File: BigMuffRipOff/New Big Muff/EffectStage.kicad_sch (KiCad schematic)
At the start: 64 parts, among them Q1 BC549, Q2 BC549, Q3 BC549, Q4 BC549, U1 TPL0501-100DCNR, U2 TPL0501-100DCNR, U3 TPL0501-100DCNR, U4 TL071HIDBVR, U5 TL071HIDBVR, U7 TL071HIDBVR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

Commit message: removed the old diodes from before
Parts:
- removed CR1, CR2: 1N4148W-13-F, 284867-E-footprint:SOD123_DIO, symbol 1N4148:1N4148W-13-F
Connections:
- net at C10.2, C9.1, Q3.1 (C)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: now also C8.1

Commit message: big muff connector fixed i think?
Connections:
- net CS_1 renamed sustain_CS
- net CS_2 renamed tone_CS
- net CS_3 renamed volume_CS_1
- net CS_4 renamed Volume_CS_2
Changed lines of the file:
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@@
 		)
 	)
-	(hierarchical_label "CS_1"
+	(hierarchical_label "sustain_CS"
 		(shape input)
 		(at 134.62 85.09 180)
@@
 		)
 	)
-	(hierarchical_label "CS_2"
+	(hierarchical_label "tone_CS"
 		(shape input)
 		(at 356.87 72.39 180)
@@
 		)
 	)
-	(hierarchical_label "CS_4"
+	(hierarchical_label "Volume_CS_2"
 		(shape input)
 		(at 447.04 143.51 180)
@@
 		)
 	)
-	(hierarchical_label "CS_3"
+	(hierarchical_label "volume_CS_1"
 		(shape input)
 		(at 445.77 90.17 180)

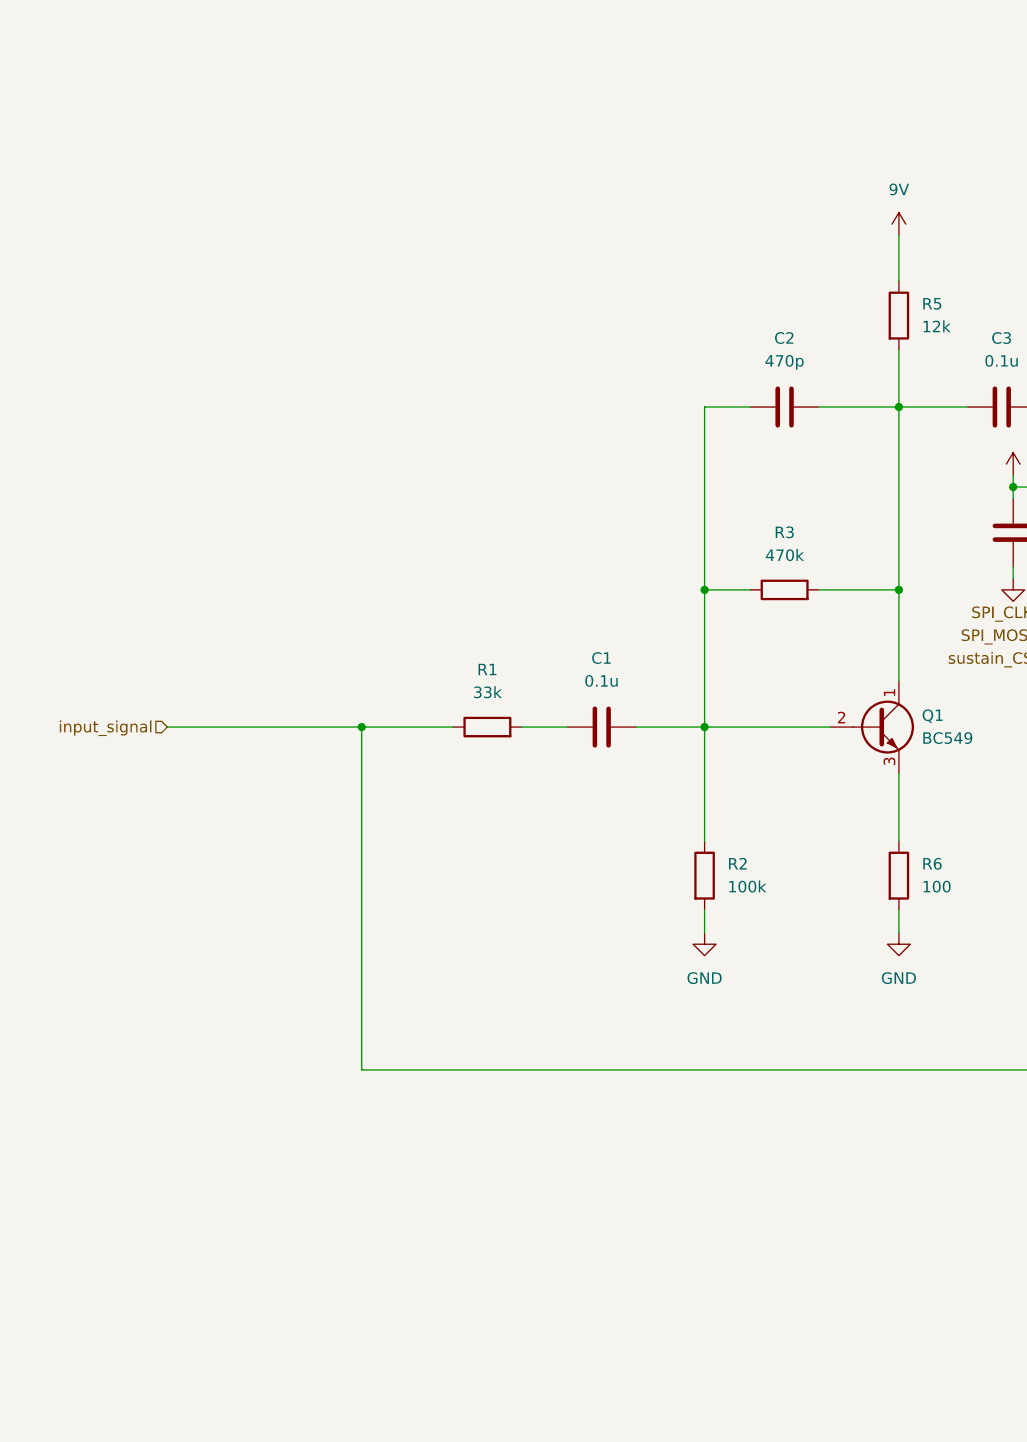
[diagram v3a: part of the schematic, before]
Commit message: added buffer to big muff
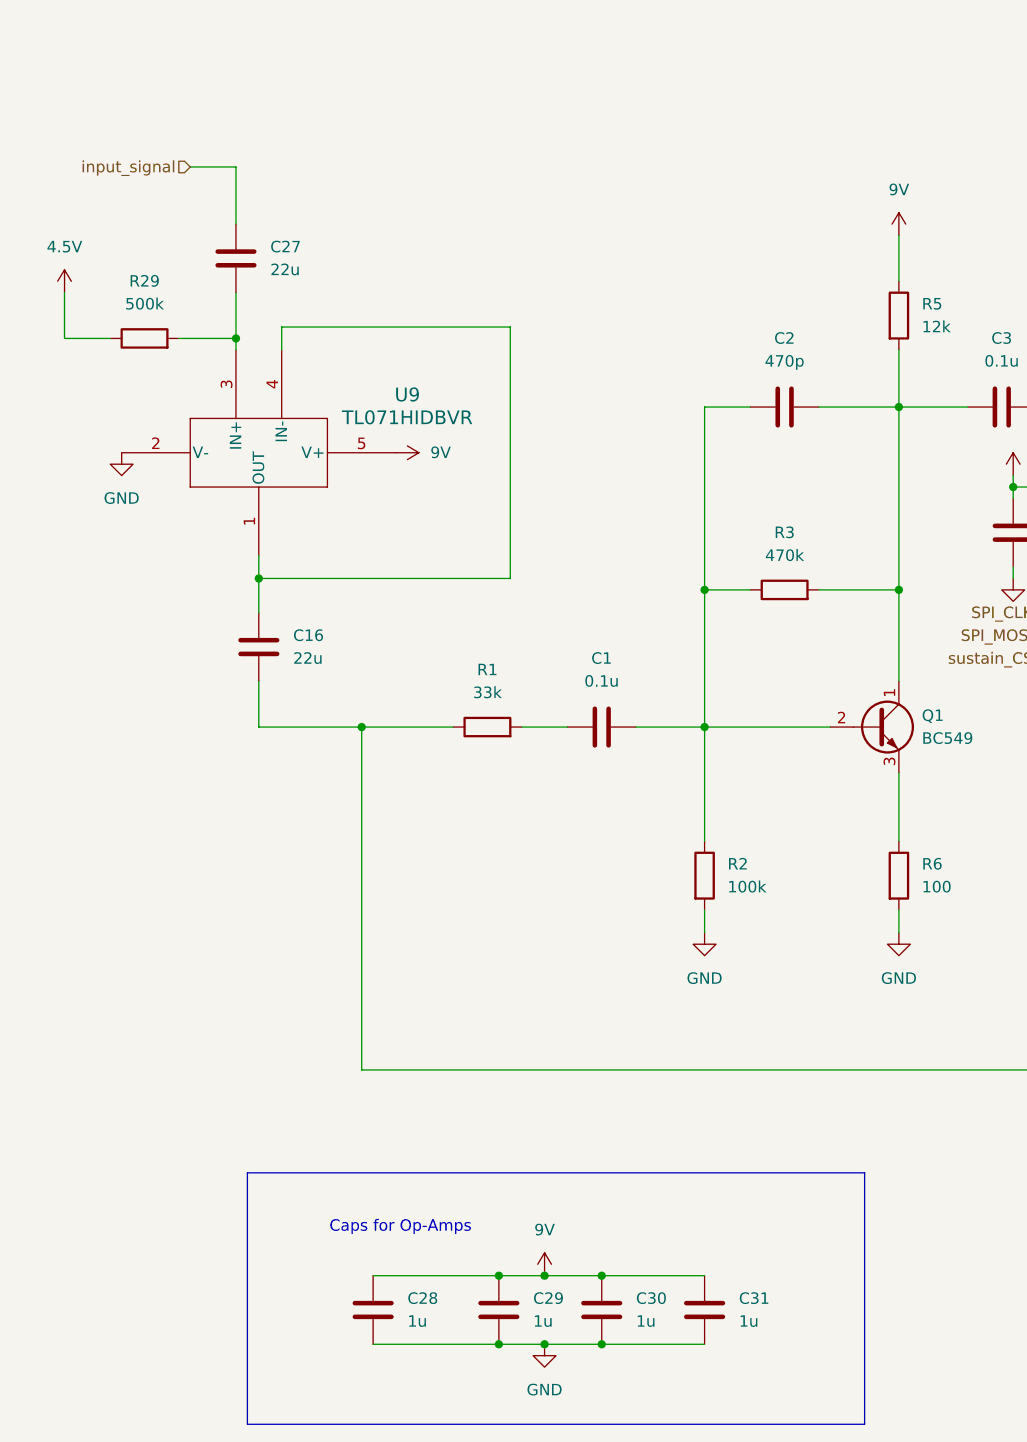
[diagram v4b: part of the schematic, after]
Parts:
- added C16, C27: 22u, Capacitor_SMD:C_0603_1608Metric, symbol Device:C
- added C28, C29, C30, C31: 1u, Capacitor_SMD:C_0603_1608Metric, symbol Device:C
- added R29: 500k, Resistor_SMD:R_0603_1608Metric, symbol Device:R
- added U9: TL071HIDBVR, 284867-E-footprint:SOT23_DBV_5_TEX, symbol TL071HIDBVR:TL071HIDBVR
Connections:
- net 4.5V: now also R29.1
- net 9V: now also C28.1, C29.1, C30.1, C31.1, U9.5 (V+)
- net GND: now also C28.2, C29.2, C30.2, C31.2, U9.2 (V-)
- net input_signal: now also C27.1; no longer C18.2, R1.1
- new net: C16.2, C18.2, R1.1
- new net: C16.1, U9.1 (OUT), U9.4 (IN-)
- new net: C27.2, R29.2, U9.3 (IN+)
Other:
- note added: "Caps for Op-Amps"
